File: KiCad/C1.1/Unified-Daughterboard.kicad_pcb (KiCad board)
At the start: 2 copper layers, 18 x 16.5 mm, 8 parts, among them J1 HRO-TYPE-C-31-M-12, J2 Conn_01x04

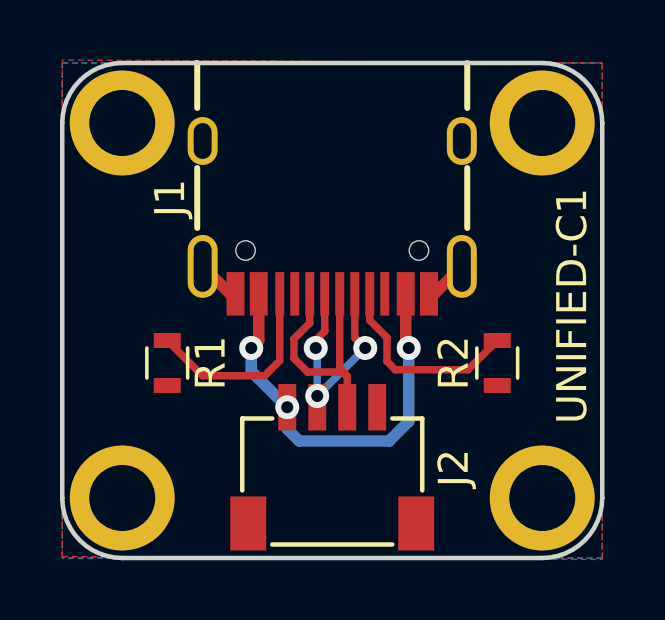
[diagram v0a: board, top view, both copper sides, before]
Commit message: Move vias off of pads
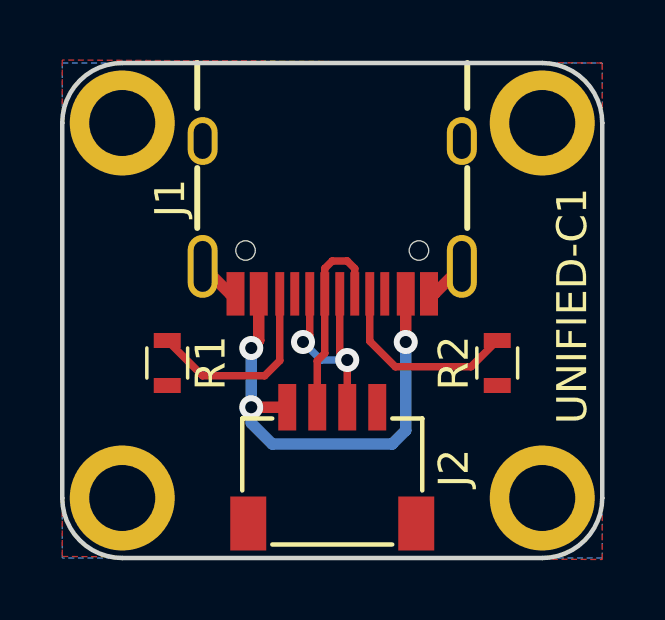
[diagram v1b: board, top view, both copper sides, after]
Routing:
- net VCC: track 13.9 -> 15.8 mm
- net D-: track 8.14 -> 6.78 mm, vias 3 -> 0
- net D+: track 8.28 -> 7.31 mm, vias 0 -> 2
